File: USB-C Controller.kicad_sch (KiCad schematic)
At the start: 0 parts

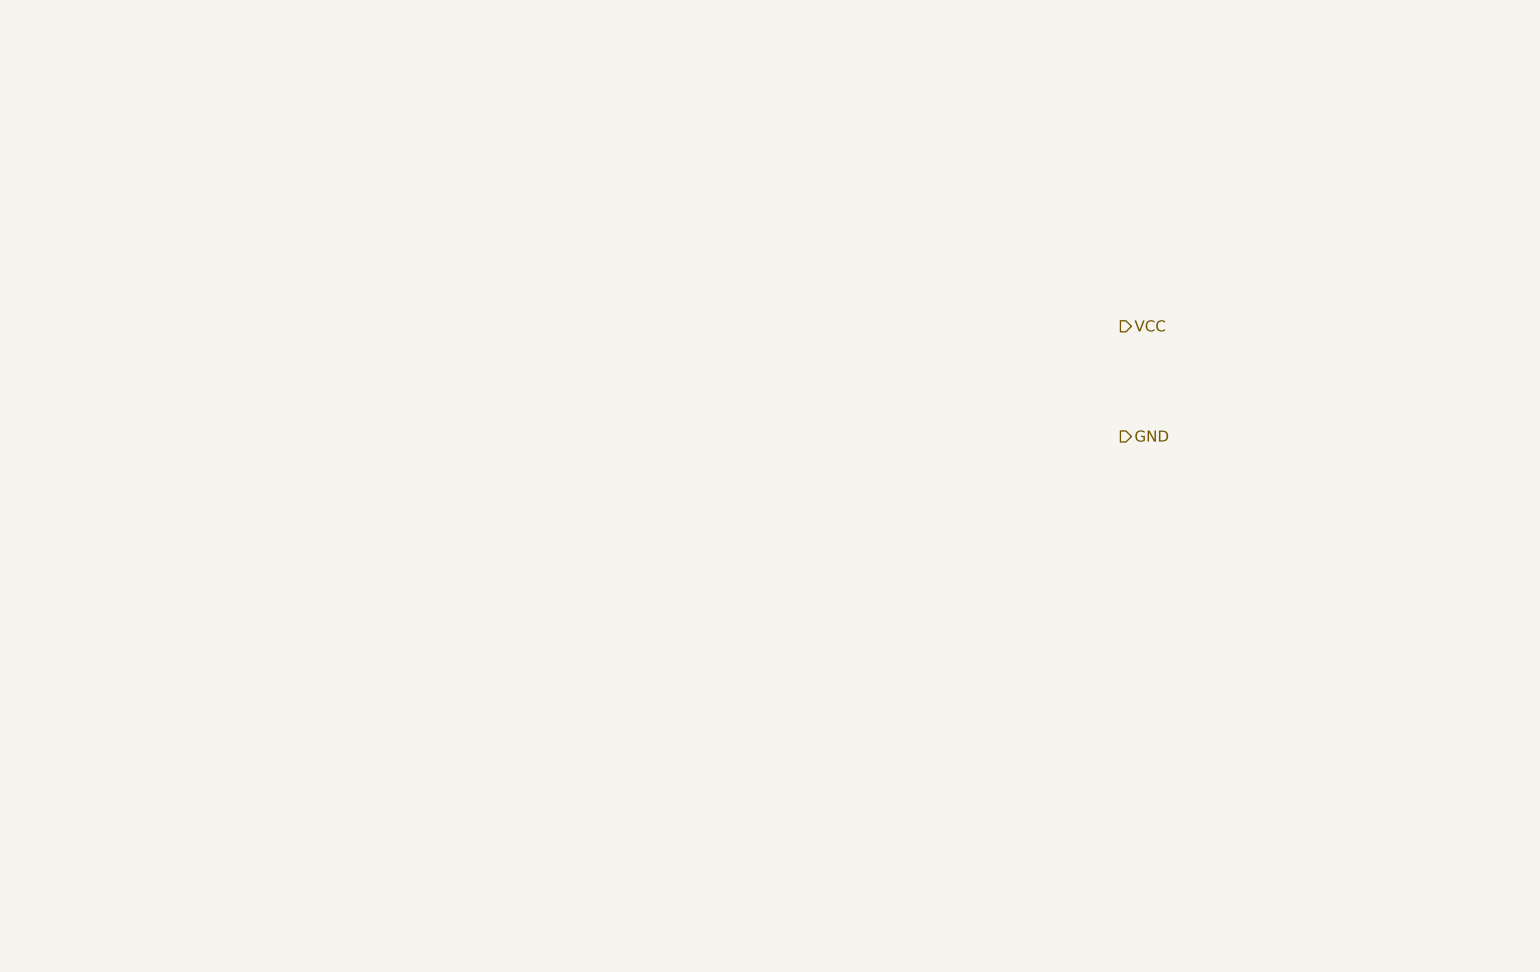
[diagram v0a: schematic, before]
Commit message: Specify LED, resistors, and start on USB-C circuit
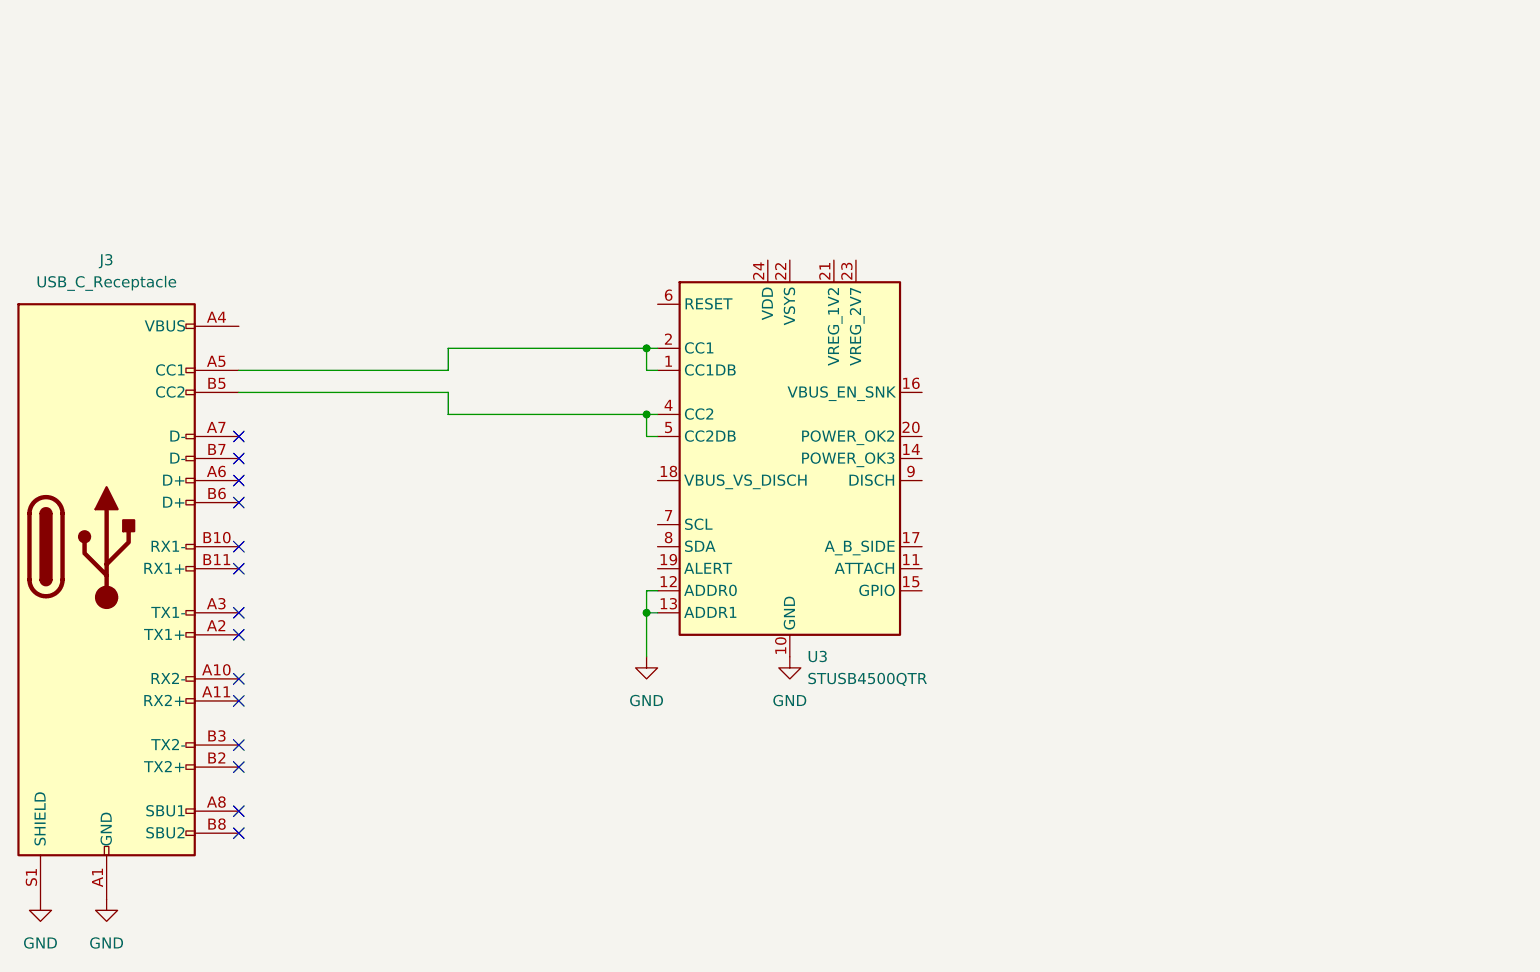
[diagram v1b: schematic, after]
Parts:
- added J3: USB_C_Receptacle, Connector_USB:USB_C_Receptacle_HRO_TYPE-C-31-M-12, symbol Connector:USB_C_Receptacle
- added U3: STUSB4500QTR, Package_DFN_QFN:QFN-24-1EP_4x4mm_P0.5mm_EP2.7x2.7mm, symbol Interface_USB:STUSB4500QTR
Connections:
- net GND: now also J3.A1 (GND), J3.A12 (GND), J3.B1 (GND), J3.B12 (GND), J3.S1 (SHIELD), U3.10 (GND), U3.12 (ADDR0), U3.13 (ADDR1), U3.25 (GND)
- new net: J3.A5 (CC1), U3.1 (CC1DB), U3.2 (CC1)
- new net: J3.B5 (CC2), U3.4 (CC2), U3.5 (CC2DB)
- new net: J3.A4 (VBUS), J3.A9 (VBUS), J3.B4 (VBUS), J3.B9 (VBUS)
- no-connect marks 0 -> 14
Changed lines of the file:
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@@
 (kicad_sch (version 20211123) (generator eeschema)
   (paper "A4")
-  (hierarchical_label "VCC" (shape output) (at 194.31 95.25 0)
-    (effects (font (size 1.27 1.27)) (justify left))
-  )
-  (hierarchical_label "GND" (shape output) (at 194.31 107.95 0)
-    (effects (font (size 1.27 1.27)) (justify left))
+  (junction (at 139.7 97.79) (diameter 0) (color 0 0 0 0)
+  )
+  (junction (at 139.7 105.41) (diameter 0) (color 0 0 0 0)
+  )
+  (junction (at 139.7 128.27) (diameter 0) (color 0 0 0 0)
+  )
+  (no_connect (at 92.71 151.13))
+  (no_connect (at 92.71 153.67))
+  (no_connect (at 92.71 130.81))
+  (no_connect (at 92.71 128.27))
+  (no_connect (at 92.71 135.89))
+  (no_connect (at 92.71 115.57))
+  (no_connect (at 92.71 110.49))
+  (no_connect (at 92.71 113.03))
+  (no_connect (at 92.71 120.65))
+  (no_connect (at 92.71 123.19))
+  (no_connect (at 92.71 143.51))
+  (no_connect (at 92.71 146.05))
+  (no_connect (at 92.71 138.43))
+  (no_connect (at 92.71 107.95))
+  (wire (pts (xy 139.7 107.95) (xy 139.7 105.41))
+    (stroke (width 0) (type default) (color 0 0 0 0))
+  )
+  (wire (pts (xy 139.7 133.35) (xy 139.7 128.27))
+    (stroke (width 0) (type default) (color 0 0 0 0))
+  )
+  (wire (pts (xy 139.7 128.27) (xy 139.7 125.73))
+    (stroke (width 0) (type default) (color 0 0 0 0))
+  )
+  (wire (pts (xy 139.7 128.27) (xy 140.97 128.27))
+    (stroke (width 0) (type default) (color 0 0 0 0))
+  )
+  (wire (pts (xy 139.7 97.79) (xy 140.97 97.79))
+    (stroke (width 0) (type default) (color 0 0 0 0))
+  )
+  (wire (pts (xy 116.84 105.41) (xy 139.7 105.41))
+    (stroke (width 0) (type default) (color 0 0 0 0))
+  )
+  (wire (pts (xy 116.84 100.33) (xy 116.84 97.79))
+    (stroke (width 0) (type default) (color 0 0 0 0))
+  )
+  (wire (pts (xy 116.84 97.79) (xy 139.7 97.79))
+    (stroke (width 0) (type default) (color 0 0 0 0))
+  )
+  (wire (pts (xy 139.7 105.41) (xy 140.97 105.41))
+    (stroke (width 0) (type default) (color 0 0 0 0))
+  )
+  (wire (pts (xy 92.71 100.33) (xy 116.84 100.33))
+    (stroke (width 0) (type default) (color 0 0 0 0))
+  )
+  (wire (pts (xy 139.7 125.73) (xy 140.97 125.73))
+    (stroke (width 0) (type default) (color 0 0 0 0))
+  )
+  (wire (pts (xy 140.97 107.95) (xy 139.7 107.95))
+    (stroke (width 0) (type default) (color 0 0 0 0))
+  )
+  (wire (pts (xy 140.97 100.33) (xy 139.7 100.33))
+    (stroke (width 0) (type default) (color 0 0 0 0))
+  )
+  (wire (pts (xy 116.84 102.87) (xy 116.84 105.41))
+    (stroke (width 0) (type default) (color 0 0 0 0))
+  )
+  (wire (pts (xy 139.7 100.33) (xy 139.7 97.79))
+    (stroke (width 0) (type default) (color 0 0 0 0))
+  )
+  (wire (pts (xy 92.71 102.87) (xy 116.84 102.87))
+    (stroke (width 0) (type default) (color 0 0 0 0))
+  )
+  (symbol (lib_id "power:GND") (at 156.21 133.35 0) (unit 1)
+    (in_bom yes) (on_board yes) (fields_autoplaced)
+    (property "Reference" "#PWR0120" (id 0) (at 156.21 139.7 0)
+      (effects (font (size 1.27 1.27)) hide)
+    )
+    (property "Value" "GND" (id 1) (at 156.21 138.43 0))
+    (property "Footprint" "" (id 2) (at 156.21 133.35 0)
+      (effects (font (size 1.27 1.27)) hide)
+    )
+    (property "Datasheet" "" (id 3) (at 156.21 133.35 0)
+      (effects (font (size 1.27 1.27)) hide)
+    )
+    (pin "1")
+  )
+  (symbol (lib_id "Interface_USB:STUSB4500QTR") (at 156.21 110.49 0) (unit 1)
+    (in_bom yes) (on_board yes) (fields_autoplaced)
+    (property "Reference" "U3" (id 0) (at 158.2294 133.35 0)
+      (effects (font (size 1.27 1.27)) (justify left))
+    )
+    (property "Value" "STUSB4500QTR" (id 1) (at 158.2294 135.89 0)
+      (effects (font (size 1.27 1.27)) (justify left))
+    )
+    (property "Footprint" "Package_DFN_QFN:QFN-24-1EP_4x4mm_P0.5mm_EP2.7x2.7mm" (id 2) (at 156.21 110.49 0)
+      (effects (font (size 1.27 1.27)) hide)
+    )
+    (property "Datasheet" "https://www.st.com/resource/en/datasheet/stusb4500.pdf" (id 3) (at 156.21 110.49 0)
+      (effects (font (size 1.27 1.27)) hide)
+    )
+    (property "LCSC" "C2678061" (id 4) (at 156.21 110.49 0)
+      (effects (font (size 1.27 1.27)) hide)
+    )
+    (pin "1")
+    (pin "10")
+    (pin "11")
+    (pin "12")
+    (pin "13")
+    (pin "14")
+    (pin "15")
+    (pin "16")
+    (pin "17")
+    (pin "18")
+    (pin "19")
+    (pin "2")
+    (pin "20")
+    (pin "21")
+    (pin "22")
+    (pin "23")
+    (pin "24")
+    (pin "25")
+    (pin "3")
+    (pin "4")
+    (pin "5")
+    (pin "6")
+    (pin "7")
+    (pin "8")
+    (pin "9")
+  )
+  (symbol (lib_id "Connector:USB_C_Receptacle") (at 77.47 120.65 0) (unit 1)
+    (in_bom yes) (on_board yes) (fields_autoplaced)
+    (property "Reference" "J3" (id 0) (at 77.47 87.63 0))
+    (property "Value" "USB_C_Receptacle" (id 1) (at 77.47 90.17 0))
+    (property "Footprint" "Connector_USB:USB_C_Receptacle_HRO_TYPE-C-31-M-12" (id 2) (at 81.28 120.65 0)
+      (effects (font (size 1.27 1.27)) hide)
+    )
+    (property "Datasheet" "https://www.usb.org/sites/default/files/documents/usb_type-c.zip" (id 3) (at 81.28 120.65 0)
+      (effects (font (size 1.27 1.27)) hide)
+    )
+    (property "LCSC" "C165948" (id 4) (at 77.47 120.65 0)
+      (effects (font (size 1.27 1.27)) hide)
+    )
+    (pin "A1")
+    (pin "A10")
+    (pin "A11")
+    (pin "A12")
+    (pin "A2")
+    (pin "A3")
+    (pin "A4")
+    (pin "A5")
+    (pin "A6")
+    (pin "A7")
+    (pin "A8")
+    (pin "A9")
+    (pin "B1")
+    (pin "B10")
+    (pin "B11")
+    (pin "B12")
+    (pin "B2")
+    (pin "B3")
+    (pin "B4")
+    (pin "B5")
+    (pin "B6")
+    (pin "B7")
+    (pin "B8")
+    (pin "B9")
+    (pin "S1")
+  )
+  (symbol (lib_id "power:GND") (at 69.85 161.29 0) (unit 1)
+    (in_bom yes) (on_board yes) (fields_autoplaced)
+    (property "Reference" "#PWR?" (id 0) (at 69.85 167.64 0)
+      (effects (font (size 1.27 1.27)) hide)
+    )
+    (property "Value" "GND" (id 1) (at 69.85 166.37 0))
+    (property "Footprint" "" (id 2) (at 69.85 161.29 0)
+      (effects (font (size 1.27 1.27)) hide)
+    )
+    (property "Datasheet" "" (id 3) (at 69.85 161.29 0)
+      (effects (font (size 1.27 1.27)) hide)
+    )
+    (pin "1")
+  )
+  (symbol (lib_id "power:GND") (at 139.7 133.35 0) (unit 1)
+    (in_bom yes) (on_board yes) (fields_autoplaced)
+    (property "Reference" "#PWR0119" (id 0) (at 139.7 139.7 0)
+      (effects (font (size 1.27 1.27)) hide)
+    )
+    (property "Value" "GND" (id 1) (at 139.7 138.43 0))
+    (property "Footprint" "" (id 2) (at 139.7 133.35 0)
+      (effects (font (size 1.27 1.27)) hide)
+    )
+    (property "Datasheet" "" (id 3) (at 139.7 133.35 0)
+      (effects (font (size 1.27 1.27)) hide)
+    )
+    (pin "1")
+  )
+  (symbol (lib_id "power:GND") (at 77.47 161.29 0) (unit 1)
+    (in_bom yes) (on_board yes) (fields_autoplaced)
+    (property "Reference" "#PWR?" (id 0) (at 77.47 167.64 0)
+      (effects (font (size 1.27 1.27)) hide)
+    )
+    (property "Value" "GND" (id 1) (at 77.47 166.37 0))
+    (property "Footprint" "" (id 2) (at 77.47 161.29 0)
+      (effects (font (size 1.27 1.27)) hide)
+    )
+    (property "Datasheet" "" (id 3) (at 77.47 161.29 0)
+      (effects (font (size 1.27 1.27)) hide)
+    )
+    (pin "1")
   )
 )

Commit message: Add USB-C circuit components
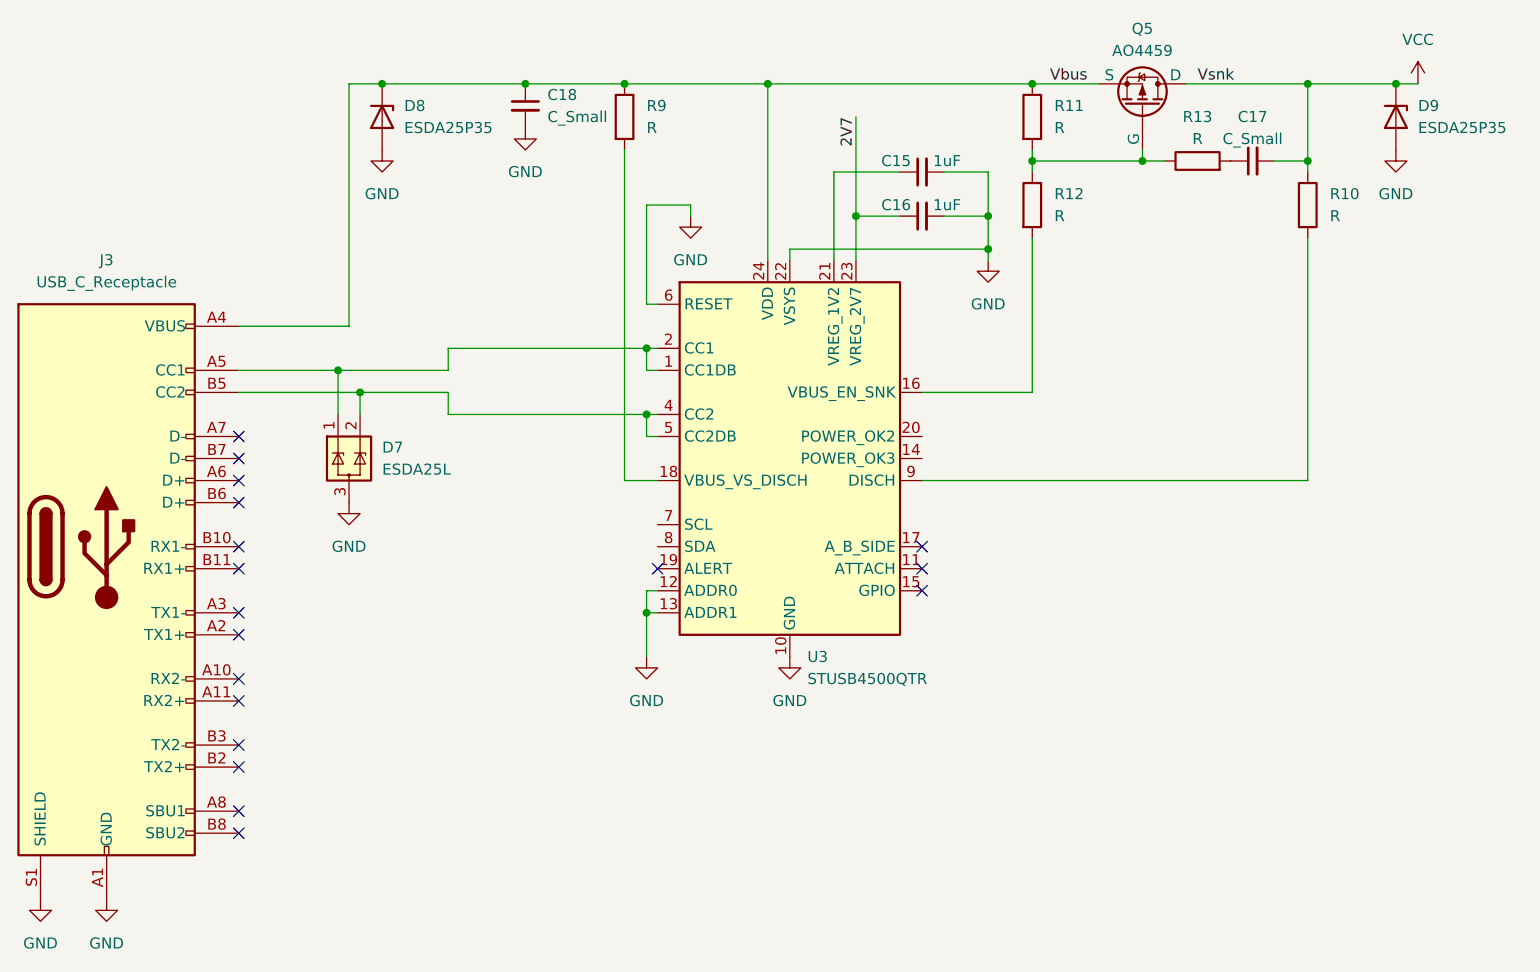
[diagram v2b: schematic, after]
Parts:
- added C15, C16: 1uF, Capacitor_SMD:C_0805_2012Metric, symbol Device:C_Small
- added C17, C18: C_Small, symbol Device:C_Small
- added D7: ESDA25L, Package_TO_SOT_SMD:SOT-23, symbol BRAUNIT Charger:ESDA25L
- added D8, D9: ESDA25P35, symbol Device:D_Zener
- added Q5: AO4459, Package_SO:SOIC-8_3.9x4.9mm_P1.27mm, symbol BRAUNIT Charger:AO4459
- added R10, R11, R12, R13, R9: R, symbol Device:R
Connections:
- net GND: now also U3.22 (VSYS), U3.6 (RESET), C15.2, C16.2, C18.2, D7.3 (GND), D8.2 (A), D9.2 (A)
- net at J3.A5 (CC1), U3.1 (CC1DB), U3.2 (CC1): now also D7.1 (IO1)
- net at U3.16 (VBUS_EN_SNK): now also R12.2
- net at U3.18 (VBUS_VS_DISCH): now also R9.2
- net at U3.21 (VREG_1V2): now also C15.1
- net 2V7: now reaches U3.23 (VREG_2V7)
- net 2V7: now also C16.1
- net Vbus: now reaches U3.24 (VDD)
- net Vbus: now also J3.A4 (VBUS), J3.A9 (VBUS), J3.B4 (VBUS), J3.B9 (VBUS), C18.1, D8.1 (K), Q5.1 (S), Q5.2 (S), Q5.3 (S), R11.1, R9.1
- net at J3.B5 (CC2), U3.4 (CC2), U3.5 (CC2DB): now also D7.2 (IO2)
- net at U3.9 (DISCH): now also R10.2
- new net: Q5.4 (G), R11.2, R12.1, R13.1
- new net: C17.1, R13.2
- new net VCC: C17.2, D9.1 (K), Q5.5 (D), Q5.6 (D), Q5.7 (D), Q5.8 (D), R10.1
- no-connect marks 14 -> 18
